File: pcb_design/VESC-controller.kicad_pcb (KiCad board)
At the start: 4 copper layers, 160 x 90 mm, 309 parts, among them J1 GATE_DRIVER_CONN_U, J2 GATE_DRIVER_CONN_V, J3 GATE_DRIVER_CONN_W, J4 micro USB, J5 ACCEL, J6 REGEN, J7 12V, J8 V_BUS, J9 SWD, P1 HALL/Encoder, P101 CANBUS, P2 Resolver, P3 PWR_COMM, Q1 BSC340N08, Q2 2N7002PW, Q3 AO4805, Q4 BC846BPDW1, Q5 BC846BPDW1, U1 STM32F40X_LQFP64, U10 LM2903-SO8, U11 LM3488, U12 OPA2376AID, U13 LM1117IMP-v.v, U14 OPA2376AID, U15 AD2S1205, U16 OPA2376AID, U17 LM2903-SO8, U18 SN74ALVC08PWR, U19 OPA2376AID, U2 ISO1050, U3 OPA2376AID, U4 LM2903-SO8, U5 7400-TSSOP, U6 SN74ALVC08PWR, U7 SN74ALVC08PWR, U8 SN74AUP1G74, U9 LM22676QTJ-5.0, X1 ABM3B - 8MHz, X2 ABM3B - 8MHz

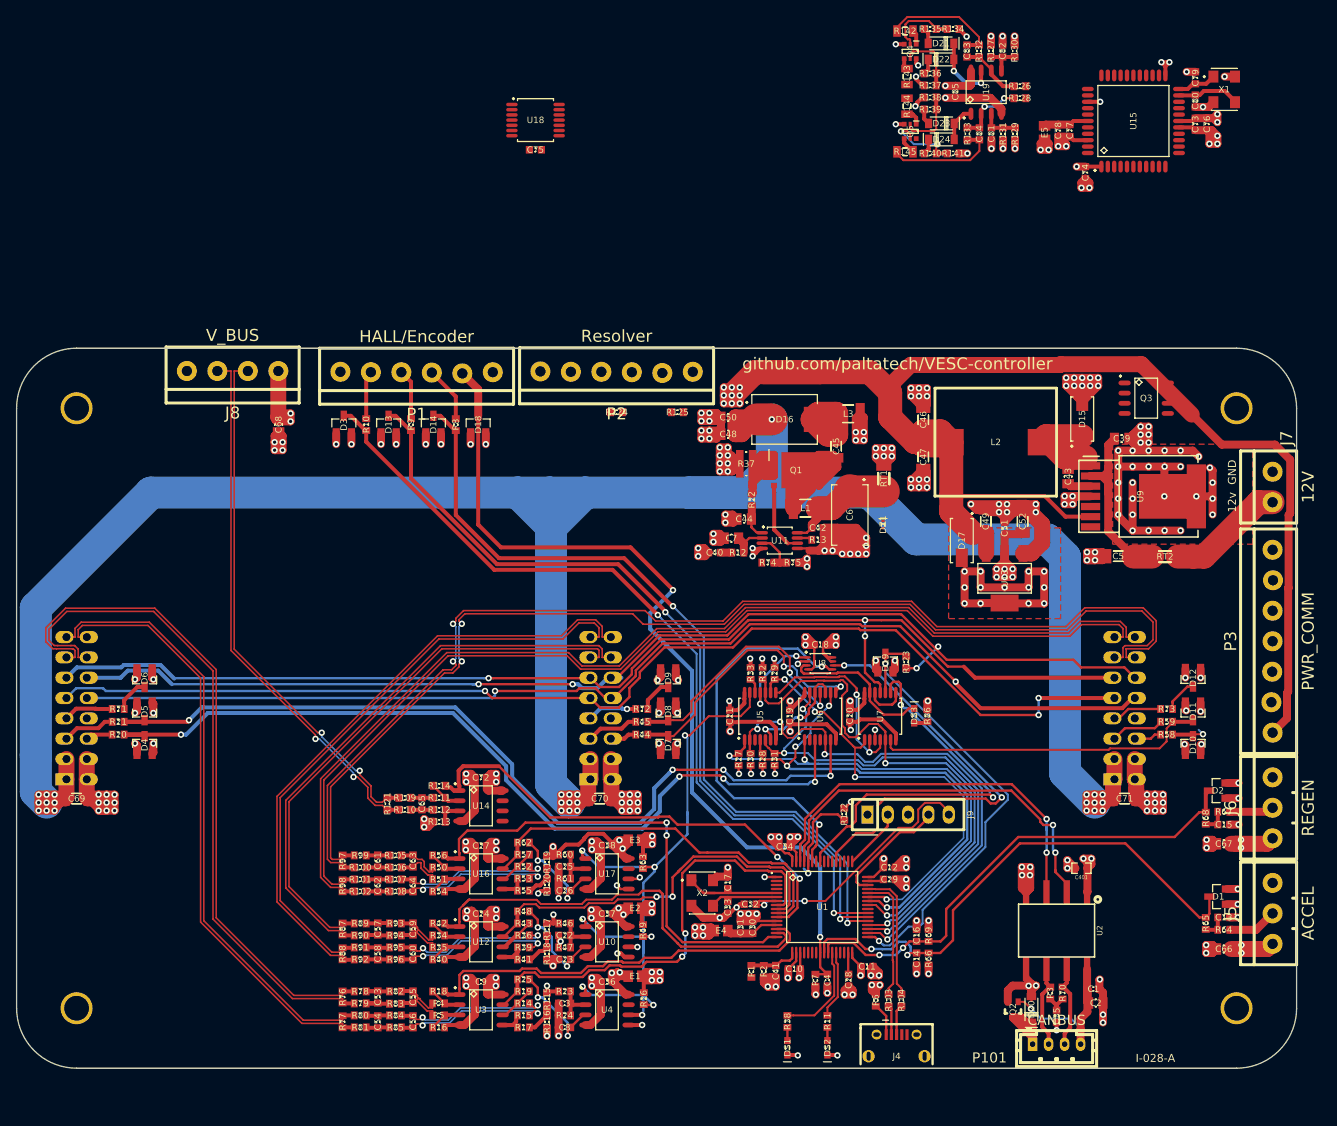
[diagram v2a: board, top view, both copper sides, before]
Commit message: Resolver routed. Added 12v regulator. The screw terminals were backwards(!). Started clearing up DRC markers.
Signed-off-by: Marcos Chaparro <mchaparro@paltatech.com>
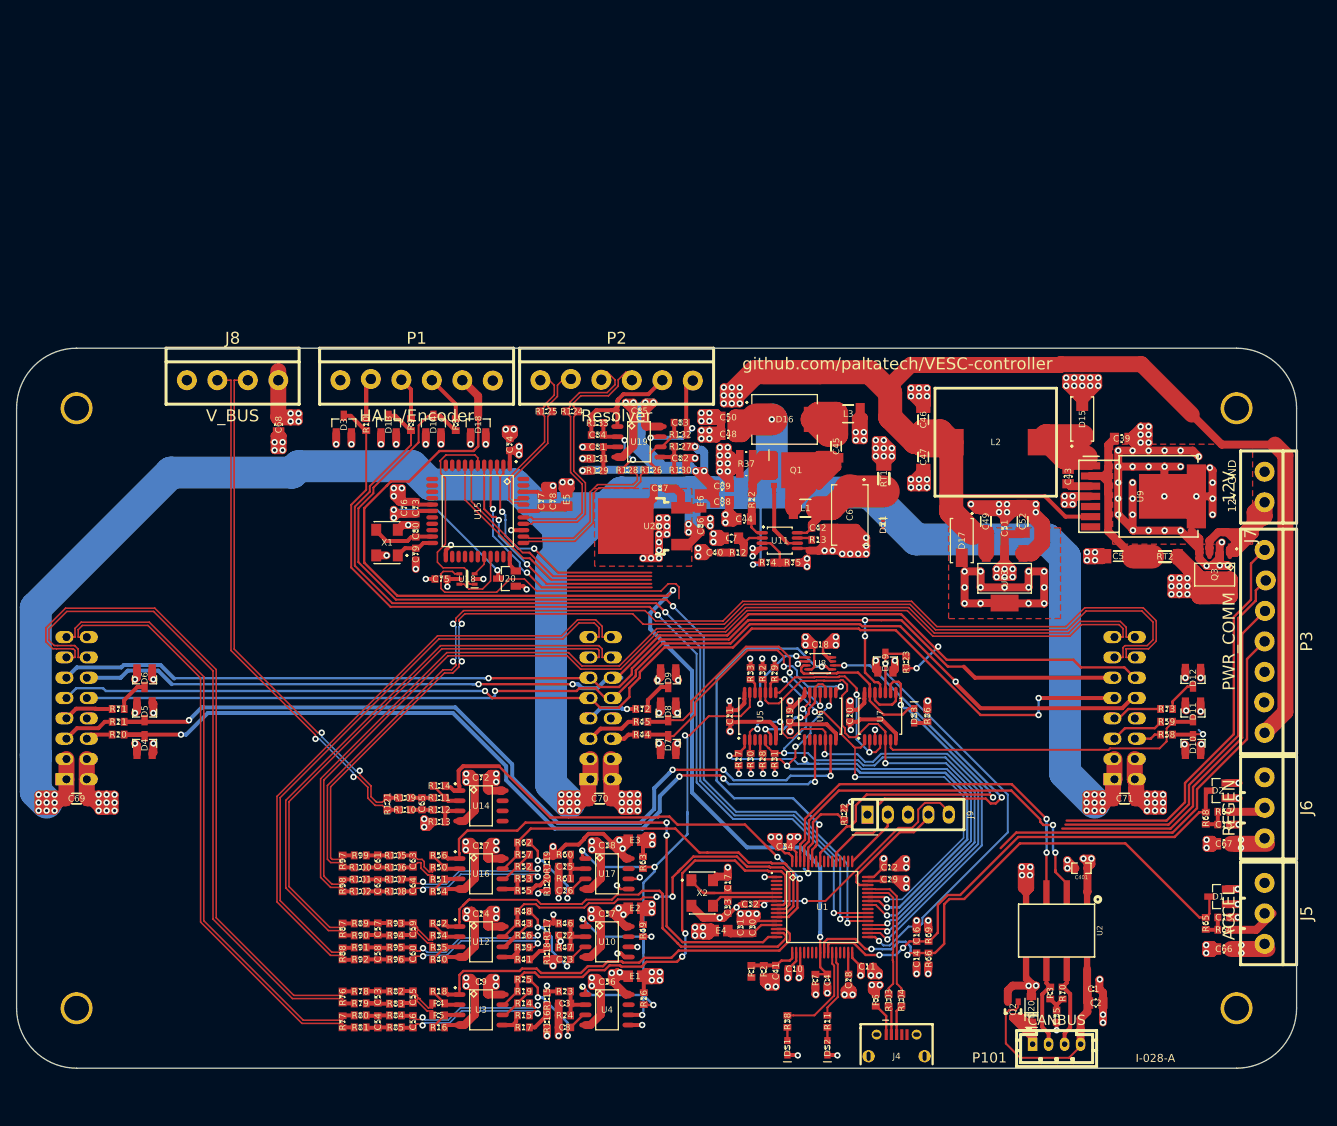
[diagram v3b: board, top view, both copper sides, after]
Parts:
- removed D21, D22, D23, D24: 1N4148W, smd-semi:SOD-123
- removed Q4, Q5: BC846BPDW1, smd-semi:SOT-363
- removed R134, R137, R138, R141: 2.2k, IPC7351-Nominal:RESC1608X50
- removed R135, R136, R139, R140: 3.3R, IPC7351-Nominal:RESC1608X50
- removed R142, R143, R144, R145: 4.7R, IPC7351-Nominal:RESC2012X50
- added C86: 100nF, IPC7351-Nominal:CAPC1608X55, F.Cu at (5.50, -22.8)
- added C87: 100nF, IPC7351-Nominal:CAPC1608X55, F.Cu at (0.40, -27.5)
- added C88: 22uF, IPC7351-Nominal:CAPC2012X70, F.Cu at (8.20, -25.8)
- added C89: 22uF, IPC7351-Nominal:CAPC2012X70, F.Cu at (8.20, -27.8)
- added E6: BEAD-220ohm@100khz, IPC7351-Nominal:INDC2012X130, F.Cu at (5.50, -25.9)
- added U20: APX809, smd-semi:SOT-23, F.Cu at (-18.7, -16.2)
- added U21: NCV78Mxx, smd-semi:TO-252, F.Cu at (-0.55, -22.8)
- C83, C84: value 100nF -> 120pF
- R127, R129: value 10k -> 22k
- R132, R133: value 10k -> 15.4k
- U18: value SN74ALVC08PWR -> AND3; footprint IPC7351-Nominal:SOP65P640X110-14 -> smd-semi:SC-70-6
- U19: value OPA2376AID -> AD8397
- moved X1 119.0 mm to (-33.7, -20.7), turned to 180 degrees
- moved C79 114.2 mm to (-30.1, -19.2), turned to 270 degrees
- moved C80 111.3 mm to (-30.1, -22.1), turned to 90 degrees
- moved C76 111.2 mm to (-31.6, -25.1), turned to 90 degrees
- moved C73 108.6 mm to (-30.1, -25.1), turned to 90 degrees
- moved U15 95.4 mm to (-22.4, -24.6), turned to 270 degrees
- moved C77 80.7 mm to (-14.4, -25.9), turned to 90 degrees
- moved C74 79.6 mm to (-18.4, -33.0), turned to 90 degrees
- moved C78 78.3 mm to (-12.9, -25.9), turned to 90 degrees
- moved E5 75.3 mm to (-11.2, -26.1), turned to 90 degrees
- moved R128 67.6 mm to (-3.70, -29.8)
- moved R129 67.1 mm to (-7.40, -29.7), turned to 180 degrees
- moved R130 67.0 mm to (2.95, -29.8), turned to 180 degrees
- moved R126 66.6 mm to (-0.70, -29.8), turned to 180 degrees
- moved R131 65.0 mm to (-7.40, -31.2), turned to 0 degrees
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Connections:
- net Net-(R126-Pad2) renamed /resolver/EXC_SOURCE+
- net Net-(R128-Pad2) renamed /resolver/EXC_SOURCE-
- J5 pad 1: +5 -> GND
- J5 pad 3: GND -> +5
- J6 pad 1: +5 -> GND
- J6 pad 3: GND -> +5
- J7 pad 1: /Power/12v_in -> GND
- J7 pad 2: GND -> /Power/12v_in
- J8 pad 1: +5 -> GND
- J8 pad 2: /V_bus+ -> /V_bus-
- J8 pad 3: /V_bus- -> /V_bus+
- J8 pad 4: GND -> +5
- P1 pad 1: +5 -> GND
- P1 pad 2: /Filters/TEMP_IN -> /Filters/HALL3_IN
- P1 pad 3: /Filters/HALL1_IN -> /Filters/HALL2_IN
- P1 pad 4: /Filters/HALL2_IN -> /Filters/HALL1_IN
- P1 pad 5: /Filters/HALL3_IN -> /Filters/TEMP_IN
- P1 pad 6: GND -> +5
- P3 pad 1: +5 -> /MISO_RX_SCL
- P3 pad 2: +3.3 -> /RX_SCL_MOSI
- P3 pad 3: GND -> /STM32F4/RX_SDA_NSS
- P3 pad 5: /STM32F4/RX_SDA_NSS -> GND
- P3 pad 6: /RX_SCL_MOSI -> +3.3
- P3 pad 7: /MISO_RX_SCL -> +5
- R127 pad 2: +5 -> +12
- R129 pad 2: +5 -> +12
- U1 pad 51: /STM32F4/PC10 -> /resolver/CLK
- U1 pad 52: /STM32F4/PC11 -> /resolver/MISO
- U1 pad 53: /Supervisor/CLR_OC_Fault -> /STM32F4/PC12
- U15 pad 2: /resolver/~RD -> /resolver/~CS
- U15 pad 4: /resolver/~SAMPLE -> /STM32F4/PB3
- U15 pad 5: /resolver/~RDVEL -> /STM32F4/PC12
- U18 pad 1: Net-(U15-Pad29) -> Net-(U15-Pad6)
- U18 pad 2: Net-(U15-Pad6) -> GND
- U18 pad 3: Net-(U18-Pad3) -> Net-(U15-Pad29)
- U18 pad 4: Net-(U15-Pad30) -> /STM32F4/PD2
- U18 pad 5: Net-(U18-Pad3) -> +3.3
- U18 pad 6: /resolver/~RES_FAULT -> Net-(U15-Pad30)
- U19 pad 1: Net-(D23-Pad1) -> /resolver/EXC-
- U19 pad 7: Net-(D21-Pad1) -> /resolver/EXC+
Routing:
- net +5: track 419.5 -> 511.7 mm, vias 24 -> 26
- net Net-(Q3-Pad5): track 5.98 -> 96.9 mm, vias 0 -> 17
- net /Power/12v_in: track 86.0 -> 28.4 mm, vias 6 -> 0
- net +12: track 9.01 -> 64.4 mm, vias 4 -> 6
- net /MISO_RX_SCL: track 0.00 -> 51.4 mm
- net /SCK_ADC_EXT: track 0.00 -> 51.0 mm
- net GND: track 652.7 -> 703.1 mm, vias 252 -> 266
- net /RX_SCL_MOSI: track 0.00 -> 48.5 mm
- net /STM32F4/RX_SDA_NSS: track 0.00 -> 45.6 mm
- net +24: track 344.3 -> 383.5 mm, vias 28 -> 31
- net /STM32F4/PD2: track 0.00 -> 37.6 mm
- net /resolver/SIN+: track 0.00 -> 32.5 mm
- net /STM32F4/PC12: track 0.00 -> 32.4 mm, vias 0 -> 2
- net /resolver/SIN-: track 0.00 -> 31.9 mm
- net /STM32F4/PB3: track 0.00 -> 31.8 mm, vias 0 -> 2
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- added copper zone on GND.Cu, net ISOGND
- removed copper zone on GND.Cu, net /Isolated CAN/GND_CAN
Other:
- net class Default: clearance 0.2 -> 0.19; trace_width 0.25 -> 0.19
- rule trace_clearance: 0.2 -> 0.19
- rule trace_min: 0.2 -> 0.19

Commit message: Routing complete. Added 3D models. No DRC errors, a few ERC warnings
Signed-off-by: Marcos Chaparro <mchaparro@paltatech.com>
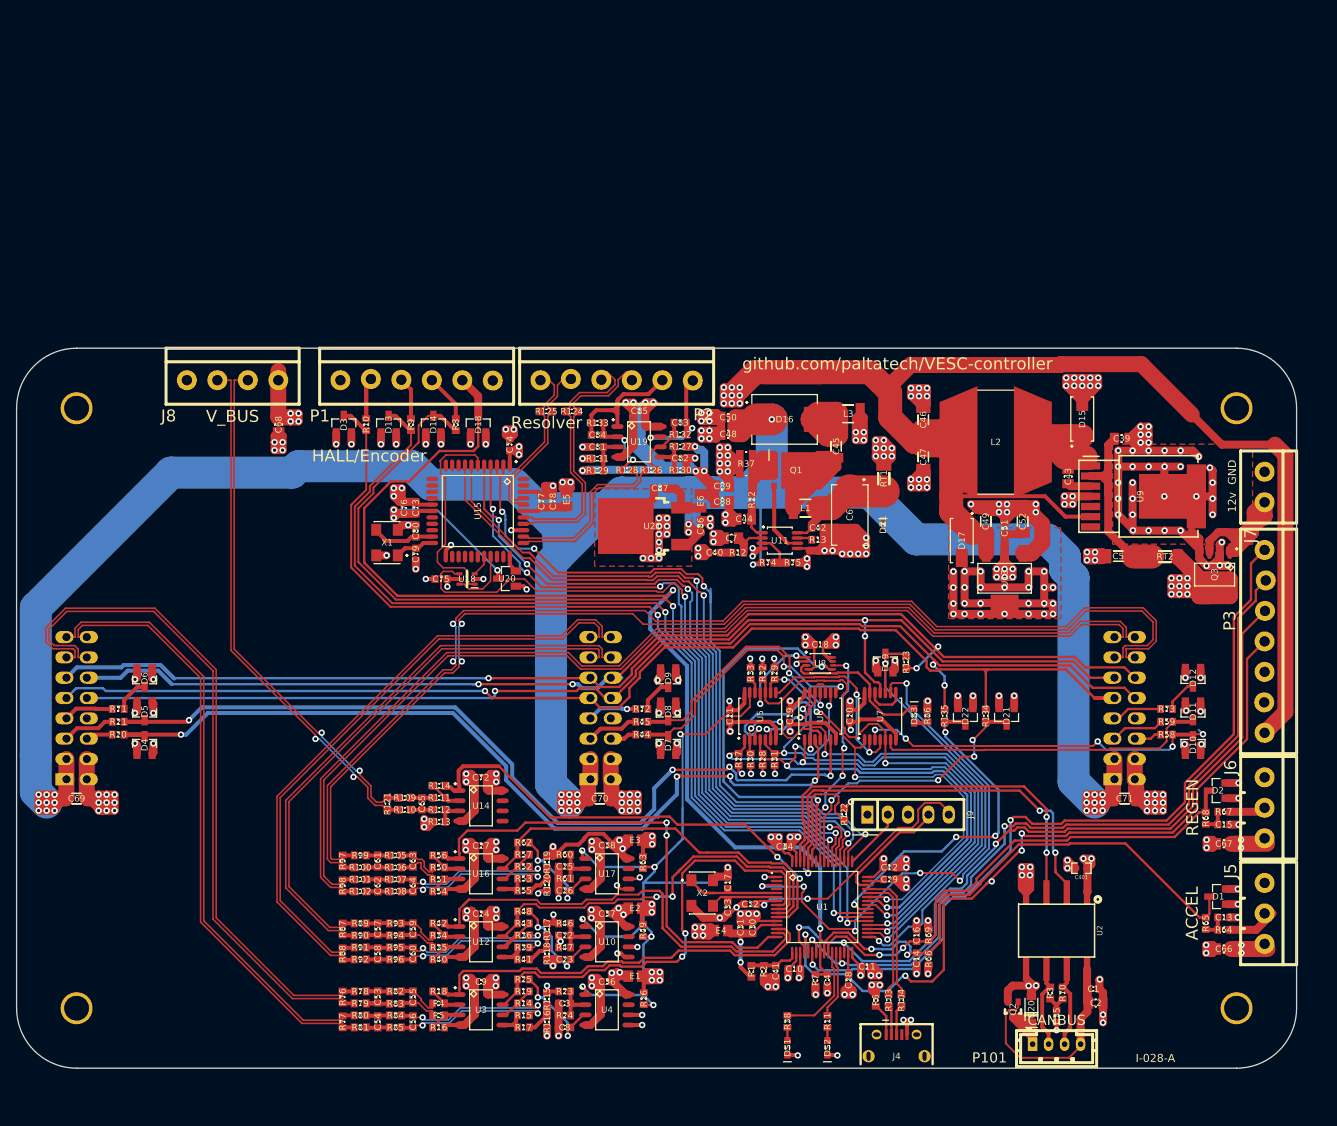
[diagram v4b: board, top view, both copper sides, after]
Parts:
- added D21: BAT54S, smd-semi:SOT-23, F.Cu at (43.8, 0.95)
- added D22: BAT54S, smd-semi:SOT-23, F.Cu at (38.6, 0.95)
- added R134: 100R, IPC7351-Nominal:RESC1608X50, F.Cu at (41.1, 0.95)
- added R135: 100R, IPC7351-Nominal:RESC1608X50, F.Cu at (36.0, 0.95)
- L2: footprint manuf:BOURNS-SRP1238A -> manuf:BOURNS-SDR1307
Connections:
- U1 pad 3: Net-(U1-Pad3) -> /STM32F4/~DRIVER_RESET
- U1 pad 40: SUPPLY_SYNC -> /STM32F4/PC9
- U1 pad 50: Net-(U1-Pad50) -> /STM32F4/SPI3_NSS
- U1 pad 56: -VEE_ctrl -> /STM32F4/PB4
- U1 pad 57: /STM32F4/~DRIVER_RESET -> /Supervisor/CLR_OC_Fault
- U15 pad 2: /resolver/~CS -> /STM32F4/SPI3_NSS
- U15 pad 3: /resolver/~CS -> /STM32F4/SPI3_NSS
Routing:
- net /STM32F4/SPI3_NSS: track 0.00 -> 91.6 mm, vias 0 -> 4
- net /resolver/MISO: track 30.9 -> 87.0 mm, vias 0 -> 2
- net /resolver/CLK: track 31.7 -> 87.7 mm, vias 0 -> 2
- net /STM32F4/PC12: track 32.4 -> 85.9 mm, vias 2 -> 4
- net /STM32F4/PB3: track 31.8 -> 83.8 mm, vias 2 -> 4
- net /STM32F4/RX_SDA_NSS: track 45.6 -> 95.4 mm, vias 0 -> 3
- net /RX_SCL_MOSI: track 48.5 -> 96.5 mm, vias 0 -> 3
- net /STM32F4/PD2: track 37.6 -> 85.4 mm, vias 0 -> 2
- net /SCK_ADC_EXT: track 51.0 -> 98.2 mm, vias 0 -> 5
- net /MISO_RX_SCL: track 51.4 -> 98.0 mm, vias 0 -> 2
- net /STM32F4/PC9: track 0.00 -> 43.3 mm, vias 0 -> 4
- net /Supervisor/PWM_GWT: track 6.01 -> 46.4 mm, vias 2 -> 5
- net /STM32F4/PB4: track 0.00 -> 36.0 mm, vias 0 -> 4
- net /resolver/~CS: track 31.0 -> 0.00 mm, vias 2 -> 0
- net /Supervisor/CLR_OC_Fault: track 53.7 -> 27.9 mm, vias 2 -> 4
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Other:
- net class Default: clearance 0.19 -> 0.17
- rule trace_clearance: 0.19 -> 0.17

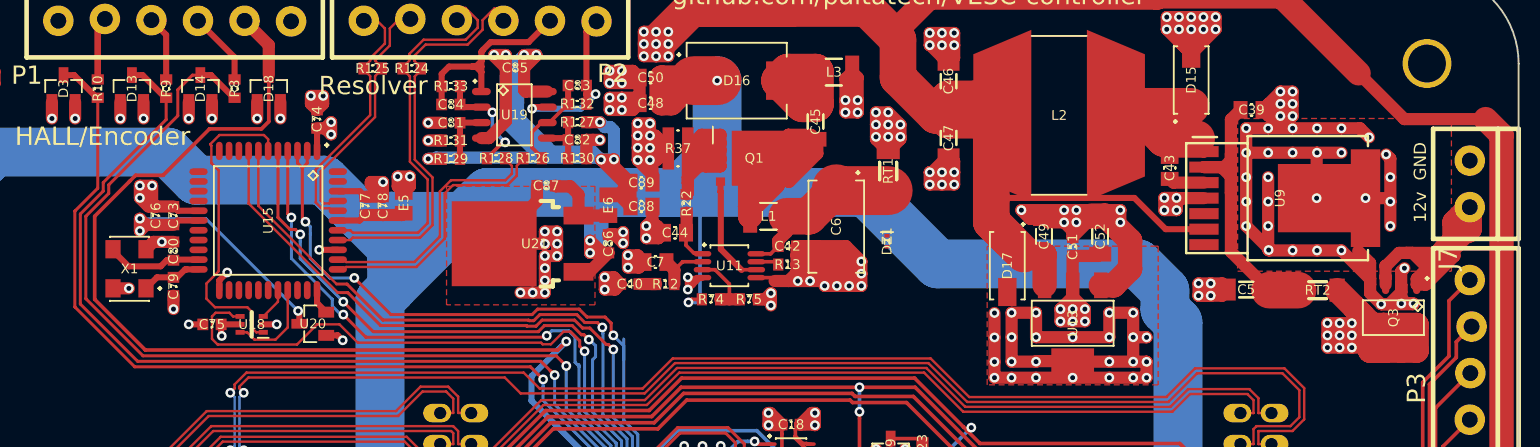
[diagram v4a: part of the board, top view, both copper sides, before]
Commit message: Added frequency set resistors for the resolver. Fixed protection mosfet installed backwards. More 3D models
Signed-off-by: Marcos Chaparro <mchaparro@paltatech.com>
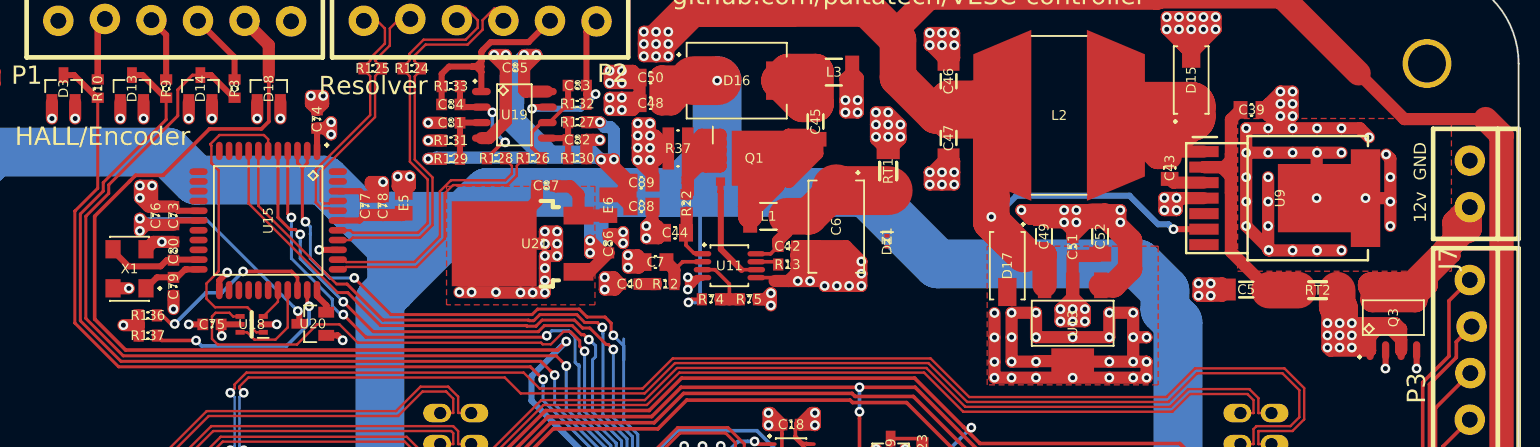
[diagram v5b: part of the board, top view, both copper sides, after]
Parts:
- added R136: 0R, IPC7351-Nominal:RESC1608X50, F.Cu at (-32.2, -16.9)
- added R137: 0R, IPC7351-Nominal:RESC1608X50, F.Cu at (-32.2, -15.2)
- turned Q3 to 90 degrees
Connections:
- Q3 pad 1: /Power/12v_in -> Net-(Q3-Pad1)
- Q3 pad 3: /Power/12v_in -> Net-(Q3-Pad1)
- Q3 pad 5: Net-(Q3-Pad5) -> /Power/12v_in
- Q3 pad 6: Net-(Q3-Pad5) -> /Power/12v_in
- Q3 pad 7: Net-(Q3-Pad5) -> /Power/12v_in
- Q3 pad 8: Net-(Q3-Pad5) -> /Power/12v_in
- RT1 pad 2: Net-(Q3-Pad5) -> Net-(Q3-Pad1)
- RT2 pad 2: Net-(Q3-Pad5) -> Net-(Q3-Pad1)
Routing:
- net Net-(Q3-Pad1): track 0.00 -> 98.5 mm, vias 0 -> 17
- net Net-(Q3-Pad5): track 96.9 -> 0.00 mm, vias 17 -> 0
- net Net-(R137-Pad2): track 0.00 -> 16.3 mm, vias 0 -> 2
- net Net-(R136-Pad2): track 0.00 -> 14.8 mm, vias 0 -> 2
- net GND: track 710.2 -> 700.5 mm, vias 270 -> 272
- net /Power/12v_in: track 28.4 -> 35.0 mm
- net Net-(C43-Pad1): track 21.2 -> 19.2 mm
- net /Filters/TEMP_IN: track 145.9 -> 146.8 mm
- net /Filters/HALL1_OUT: track 124.5 -> 125.4 mm
- net /Filters/HALL2_OUT: track 121.3 -> 122.1 mm
- net +5: track 526.6 -> 527.4 mm, vias 26 -> 28
- net /Filters/HALL3_OUT: track 118.5 -> 119.3 mm

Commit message: Moved references
Signed-off-by: Marcos Chaparro <mchaparro@paltatech.com>
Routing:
- net +24: track 383.5 -> 406.2 mm, vias 31 -> 39
- net /Filters/TEMP_IN: track 146.8 -> 147.4 mm
- net GND: vias 272 -> 273
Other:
- board text added: "OCP"
- board text added: "U"
- board text added: "V"
- board text added: "W"
